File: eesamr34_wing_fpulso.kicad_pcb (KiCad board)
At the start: 2 copper layers, 50.9 x 25.6 mm, 12 parts, among them J3 Conn_01x02_Male, P1 SolderJumper_3_Bridged12, U2 4069

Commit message: Added ibom, gerbers
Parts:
- moved J3 3.82 mm to (70.9, 37.4)
- moved R2 0.88 mm to (65.1, 44.2)
- moved U2 0.49 mm to (46.1, 41.7)
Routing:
- net /Pulso: track 65.1 -> 67.9 mm
- net GND: track 93.0 -> 94.6 mm
- net /+3.3V: track 42.8 -> 43.8 mm
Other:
- board size 50.9 x 25.6 mm -> 49.8 x 25.6 mm

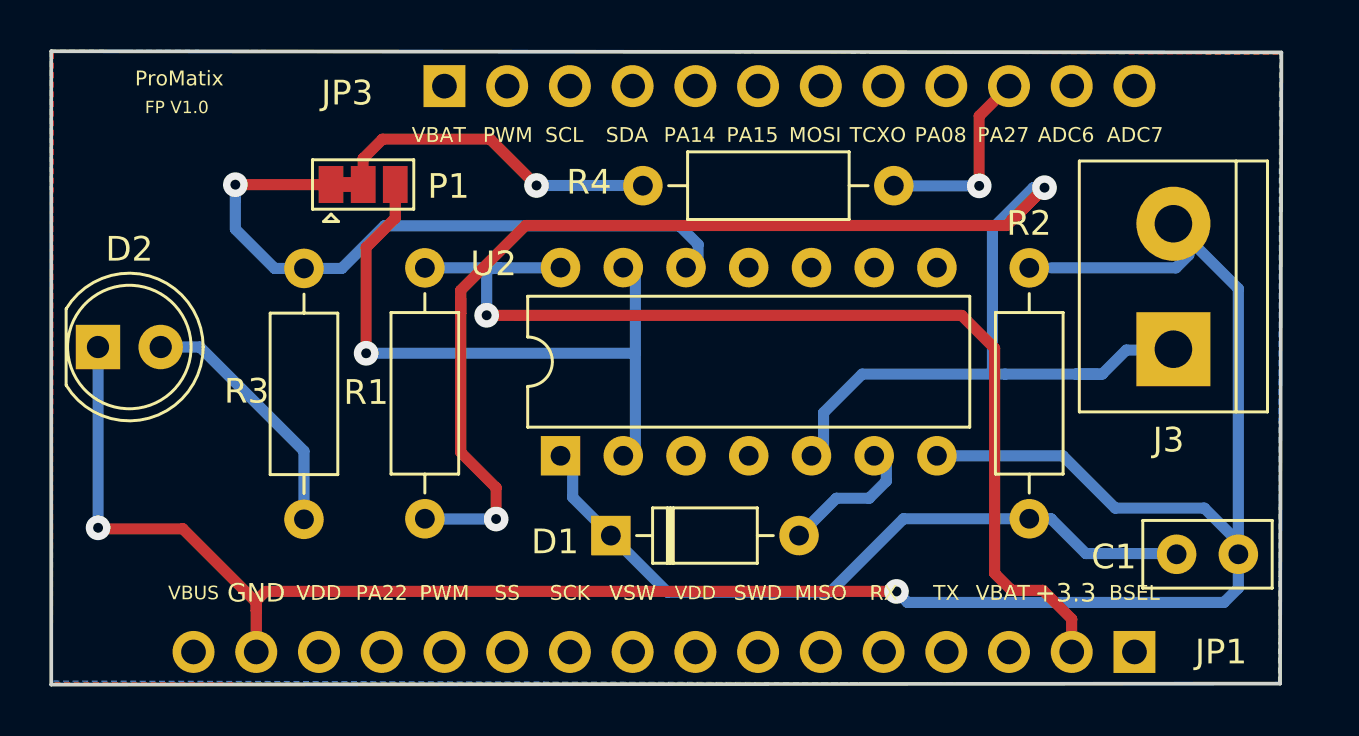
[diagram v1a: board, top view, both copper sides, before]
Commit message: Resize VIAS
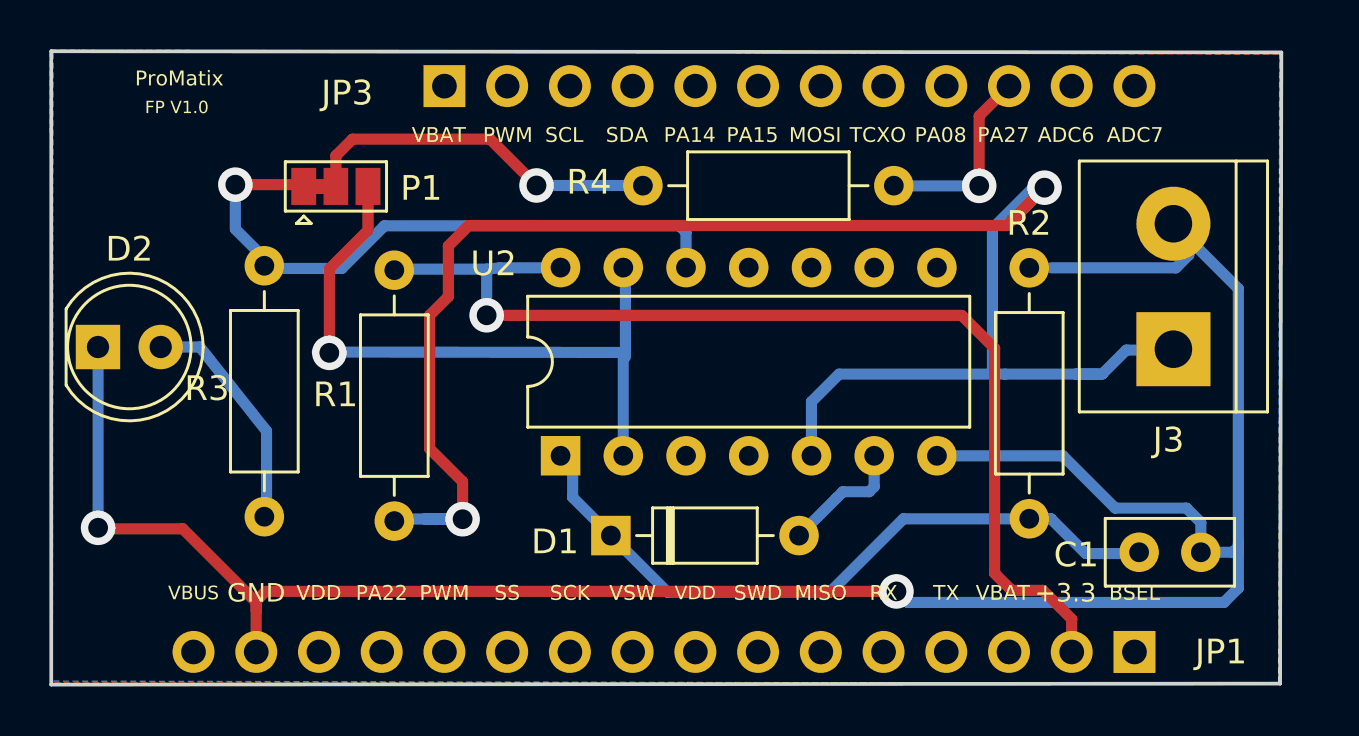
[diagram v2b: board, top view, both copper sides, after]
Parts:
- moved R3 1.61 mm to (34.1, 34.0)
- moved C1 1.52 mm to (69.5, 45.6)
- moved R1 1.24 mm to (39.3, 34.2)
- moved P1 1.11 mm to (37.0, 30.8)
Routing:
- net /Pulso: track 67.9 -> 70.9 mm
- net Net-(C1-Pad1): track 29.6 -> 28.0 mm
- net Net-(P1-Pad3): track 25.8 -> 27.3 mm
- net Net-(P1-Pad1): track 27.0 -> 25.8 mm
- net Net-(P1-Pad2): track 13.5 -> 14.7 mm
- net GND: track 94.6 -> 95.5 mm
- net Net-(D2-Pad2): track 10.3 -> 9.43 mm
- net /+3.3V: track 43.8 -> 44.6 mm
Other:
- net class Default: via_dia 1 -> 1.4; via_drill 0.4 -> 0.8

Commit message: Changed to PA08
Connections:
- R4 pad 2: /PA27 -> /PA08
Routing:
- net /PA08: track 0.00 -> 8.12 mm, vias 0 -> 1
- net /PA27: track 8.07 -> 0.00 mm, vias 1 -> 0
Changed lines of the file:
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@@
     (thickness 1.6)
     (drawings 39)
-    (tracks 127)
+    (tracks 128)
     (zones 0)
     (modules 12)
@@
       (net 33 "Net-(P1-Pad2)"))
     (pad 2 thru_hole oval (at 10.16 0) (size 1.6 1.6) (drill 0.8) (layers *.Cu *.Mask)
-      (net 18 /PA27))
+      (net 19 /PA08))
     (model ${KISYS3DMOD}/Resistor_THT.3dshapes/R_Axial_DIN0207_L6.3mm_D2.5mm_P10.16mm_Horizontal.wrl
       (at (xyz 0 0 0))
@@
   (segment (start 73.52348 45.3752) (end 73.52348 34.9231) (width 0.45) (layer B.Cu) (net 1))
   (segment (start 73.52348 45.67682) (end 73.52348 45.3752) (width 0.45) (layer B.Cu) (net 1))
-  (segment (start 59.62142 30.80004) (end 59.57316 30.75178) (width 0.25) (layer B.Cu) (net 18))
-  (segment (start 64.2366 26.7208) (end 63.0301 27.9273) (width 0.45) (layer F.Cu) (net 18))
-  (segment (start 63.0301 27.9273) (end 63.0301 30.7594) (width 0.45) (layer F.Cu) (net 18))
-  (via (at 63.0301 30.7594) (size 1.4) (drill 0.8) (layers F.Cu B.Cu) (net 18))
-  (segment (start 59.58078 30.7594) (end 59.57316 30.75178) (width 0.45) (layer B.Cu) (net 18))
-  (segment (start 63.0301 30.7594) (end 59.58078 30.7594) (width 0.45) (layer B.Cu) (net 18))
+  (segment (start 59.62142 30.80004) (end 59.57316 30.75178) (width 0.25) (layer B.Cu) (net 19))
+  (via (at 63.0301 30.7594) (size 1.4) (drill 0.8) (layers F.Cu B.Cu) (net 19))
+  (segment (start 59.58078 30.7594) (end 59.57316 30.75178) (width 0.45) (layer B.Cu) (net 19))
+  (segment (start 63.0301 30.7594) (end 59.58078 30.7594) (width 0.45) (layer B.Cu) (net 19))
+  (segment (start 63.0301 30.7594) (end 61.78042 29.50972) (width 0.45) (layer F.Cu) (net 19))
+  (segment (start 61.78042 26.80462) (end 61.6966 26.7208) (width 0.45) (layer F.Cu) (net 19))
+  (segment (start 61.78042 29.50972) (end 61.78042 26.80462) (width 0.45) (layer F.Cu) (net 19))
   (segment (start 46.56836 43.37304) (end 48.11522 44.9199) (width 0.45) (layer B.Cu) (net 27))
   (segment (start 46.56836 41.68902) (end 46.56836 43.37304) (width 0.45) (layer B.Cu) (net 27))
@@
   (segment (start 63.56604 38.38194) (end 57.35828 38.38194) (width 0.45) (layer B.Cu) (net 30))
   (via (at 32.91078 30.71114) (size 1.4) (drill 0.8) (layers F.Cu B.Cu) (net 31))
-  (segment (start 36.77714 30.71114) (end 36.78476 30.70352) (width 0.45) (layer F.Cu) (net 33))
   (segment (start 35.61128 30.71114) (end 35.6824 30.78226) (width 0.45) (layer F.Cu) (net 31))
   (segment (start 32.91078 30.71114) (end 35.61128 30.71114) (width 0.45) (layer F.Cu) (net 31))
@@
   (segment (start 36.22548 37.48786) (end 48.61814 37.50564) (width 0.45) (layer B.Cu) (net 32))
   (segment (start 48.61814 37.64026) (end 48.61814 41.68902) (width 0.45) (layer B.Cu) (net 32))
+  (segment (start 36.77714 30.71114) (end 36.78476 30.70352) (width 0.45) (layer F.Cu) (net 33))
   (via (at 45.10532 30.74416) (size 1.4) (drill 0.8) (layers F.Cu B.Cu) (net 33))
   (segment (start 49.40554 30.74416) (end 49.41316 30.75178) (width 0.45) (layer B.Cu) (net 33))
